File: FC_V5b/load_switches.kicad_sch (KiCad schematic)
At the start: 52 parts, among them U19 AP22652, U21 AP22652, U22 AP22652, U23 AP22652, U24 AP22652, U25 AP22652, U26 AP22652, U27 AP22652, U28 AP22652, U29 AP22652

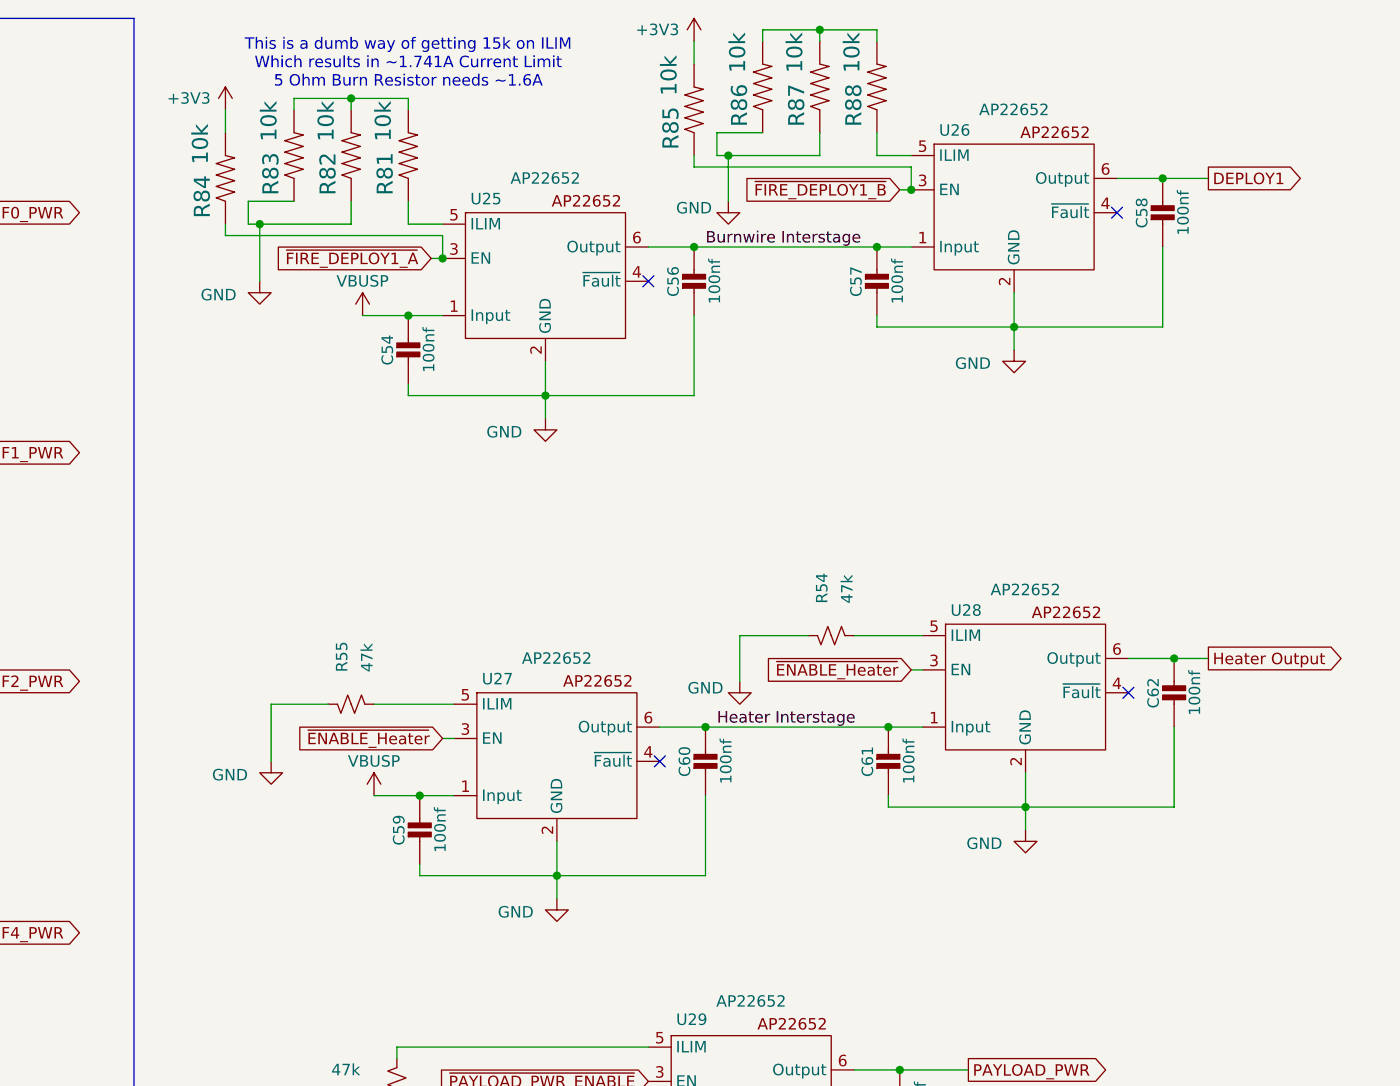
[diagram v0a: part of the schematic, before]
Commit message: Deleted Bad Heater and Burn Load Switches
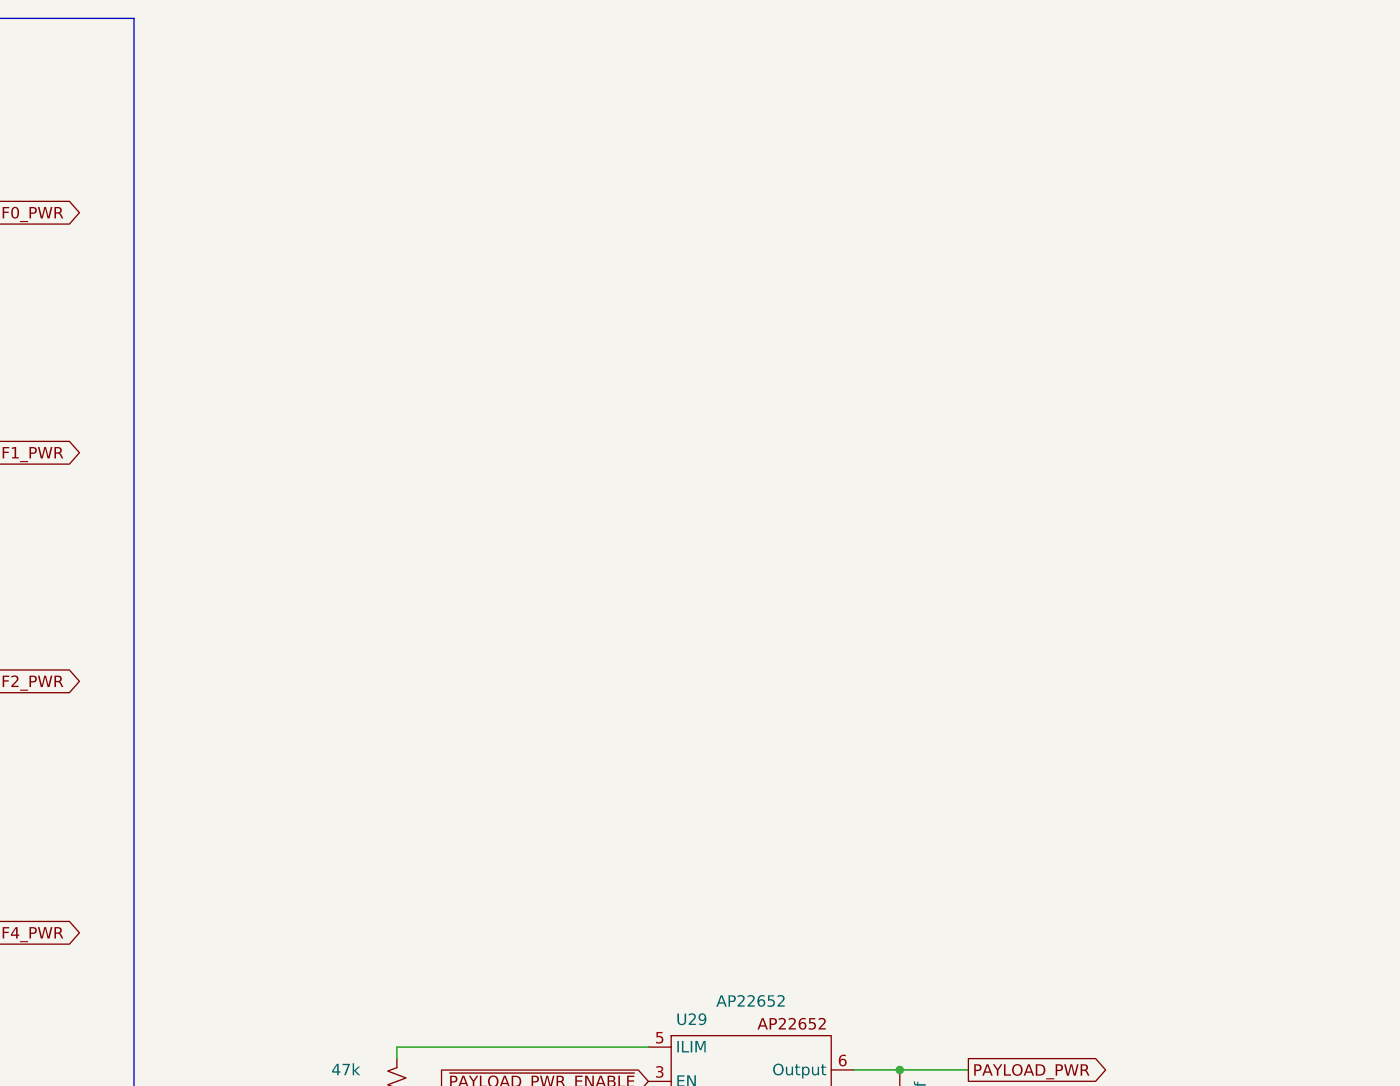
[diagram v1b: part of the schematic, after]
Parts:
- removed C54, C56, C57, C58, C59, C60, C61, C62: 100nf, Capacitor_SMD:C_0402_1005Metric, symbol Adafruit ItsyBitsy RP2040-eagle-import:CAP_CERAMIC_0402NO
- removed R54, R55: 47k, Resistor_SMD:R_0603_1608Metric, symbol Device:R_Small_US
- removed R81, R82, R83, R84, R85, R86, R87, R88: 10k, Resistor_SMD:R_0603_1608Metric, symbol mainboard:RESISTOR0603
- removed U25, U26, U27, U28: AP22652, SOT26:SOT26, symbol Power_Management:AP22652
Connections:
- no-connect marks 10 -> 6
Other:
- note removed: "This is a dumb way of getting 15k on ILIM Which results in ~1.741A Current Limit 5 Ohm Burn Resistor needs ~1.6A"

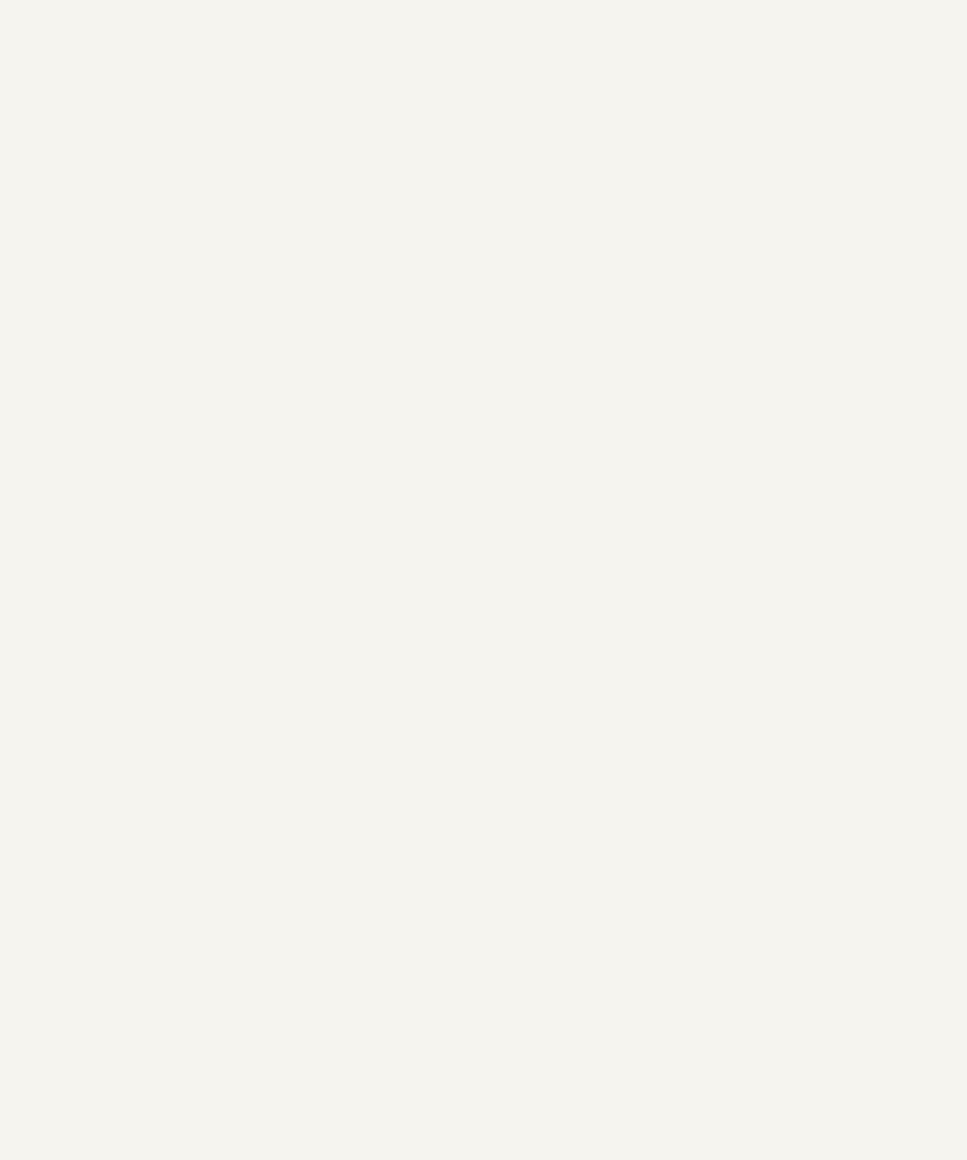
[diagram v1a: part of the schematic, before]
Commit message: Added New Load Switch Symbols
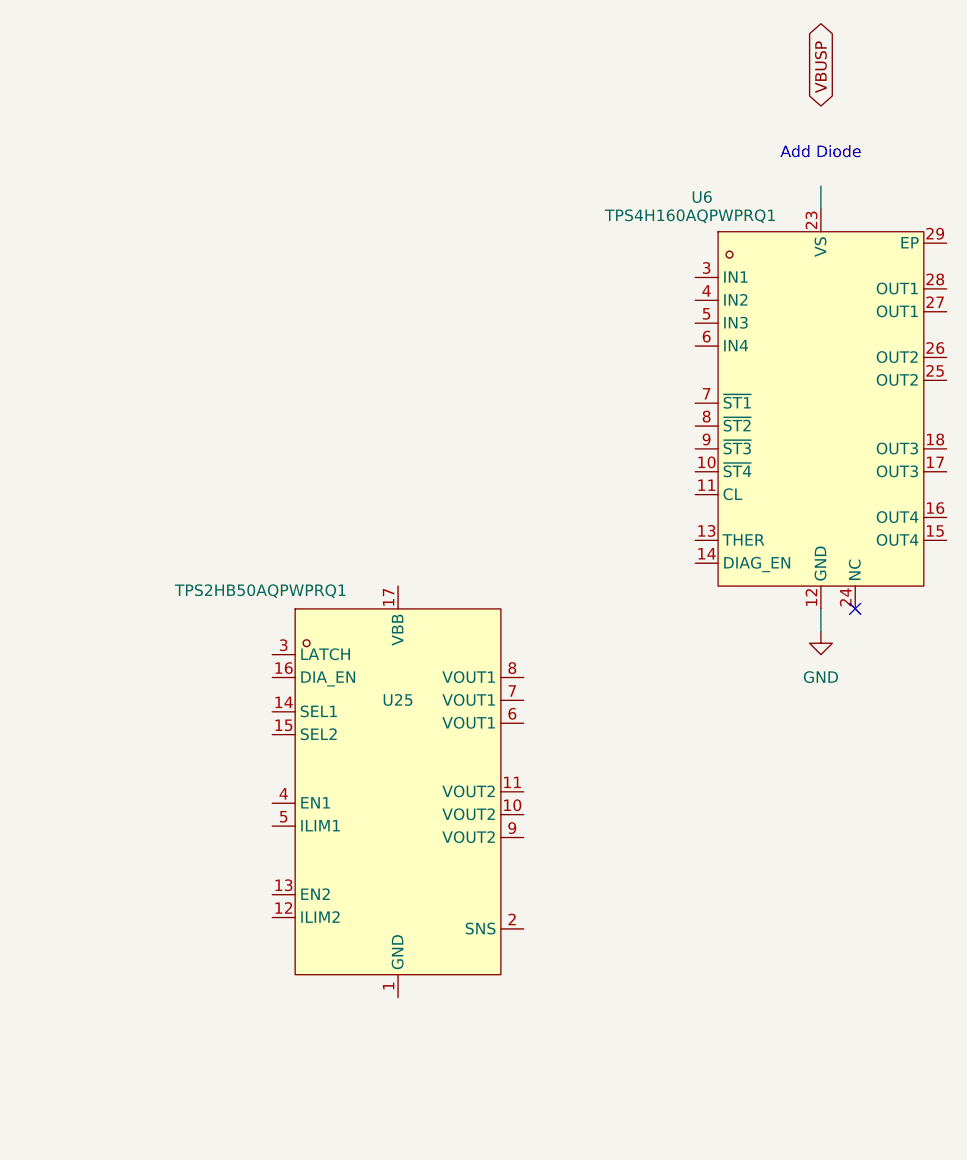
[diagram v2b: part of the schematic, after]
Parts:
- added U25: TPS2HB50AQPWPRQ1, easyeda2kicad:HTSSOP-16_L5.0-W4.4-P0.65-LS6.4-BL-EP-2, symbol easyeda2kicad:TPS2HB50AQPWPRQ1
- added U6: TPS4H160AQPWPRQ1, easyeda2kicad:HTSSOP-28_L9.7-W4.4-P0.65-LS6.4-BL-EP, symbol easyeda2kicad:TPS4H160AQPWPRQ1
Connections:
- net GND: now also U6.1 (GND), U6.12 (GND)
- new net: U6.19 (NC), U6.2 (NC), U6.24 (NC)
- new net: U6.20 (VS), U6.21 (VS), U6.22 (VS), U6.23 (VS)
- no-connect marks 6 -> 7
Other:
- note added: "Add Diode"

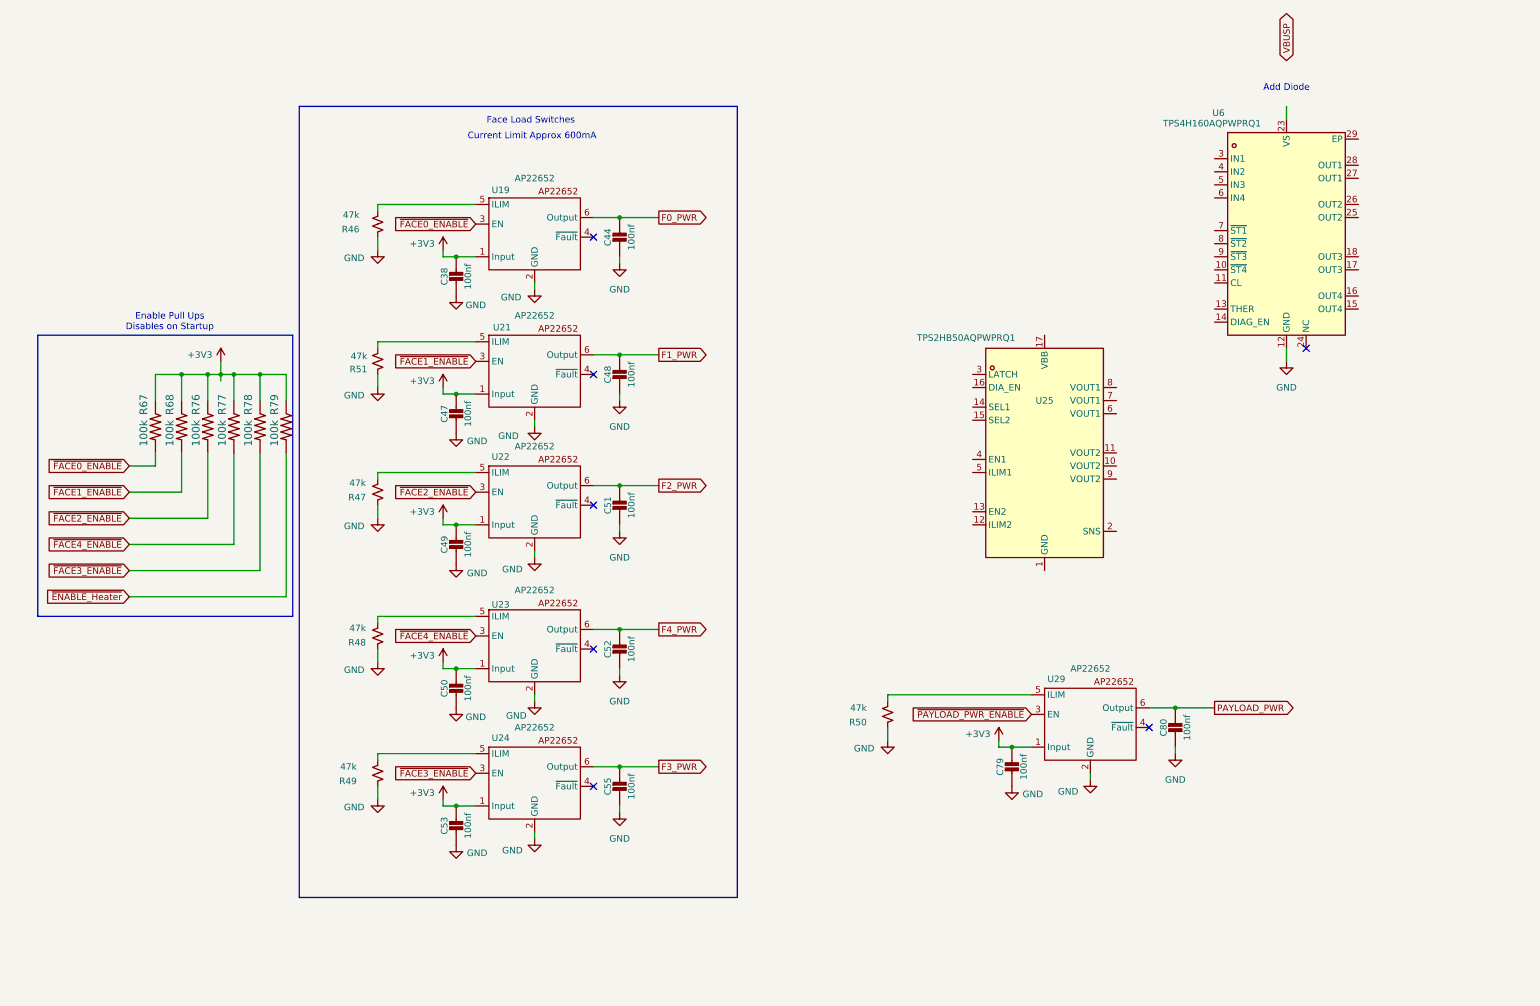
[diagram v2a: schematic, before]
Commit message: Removed Z- GPIO
Also making Progress on Load Switch Update
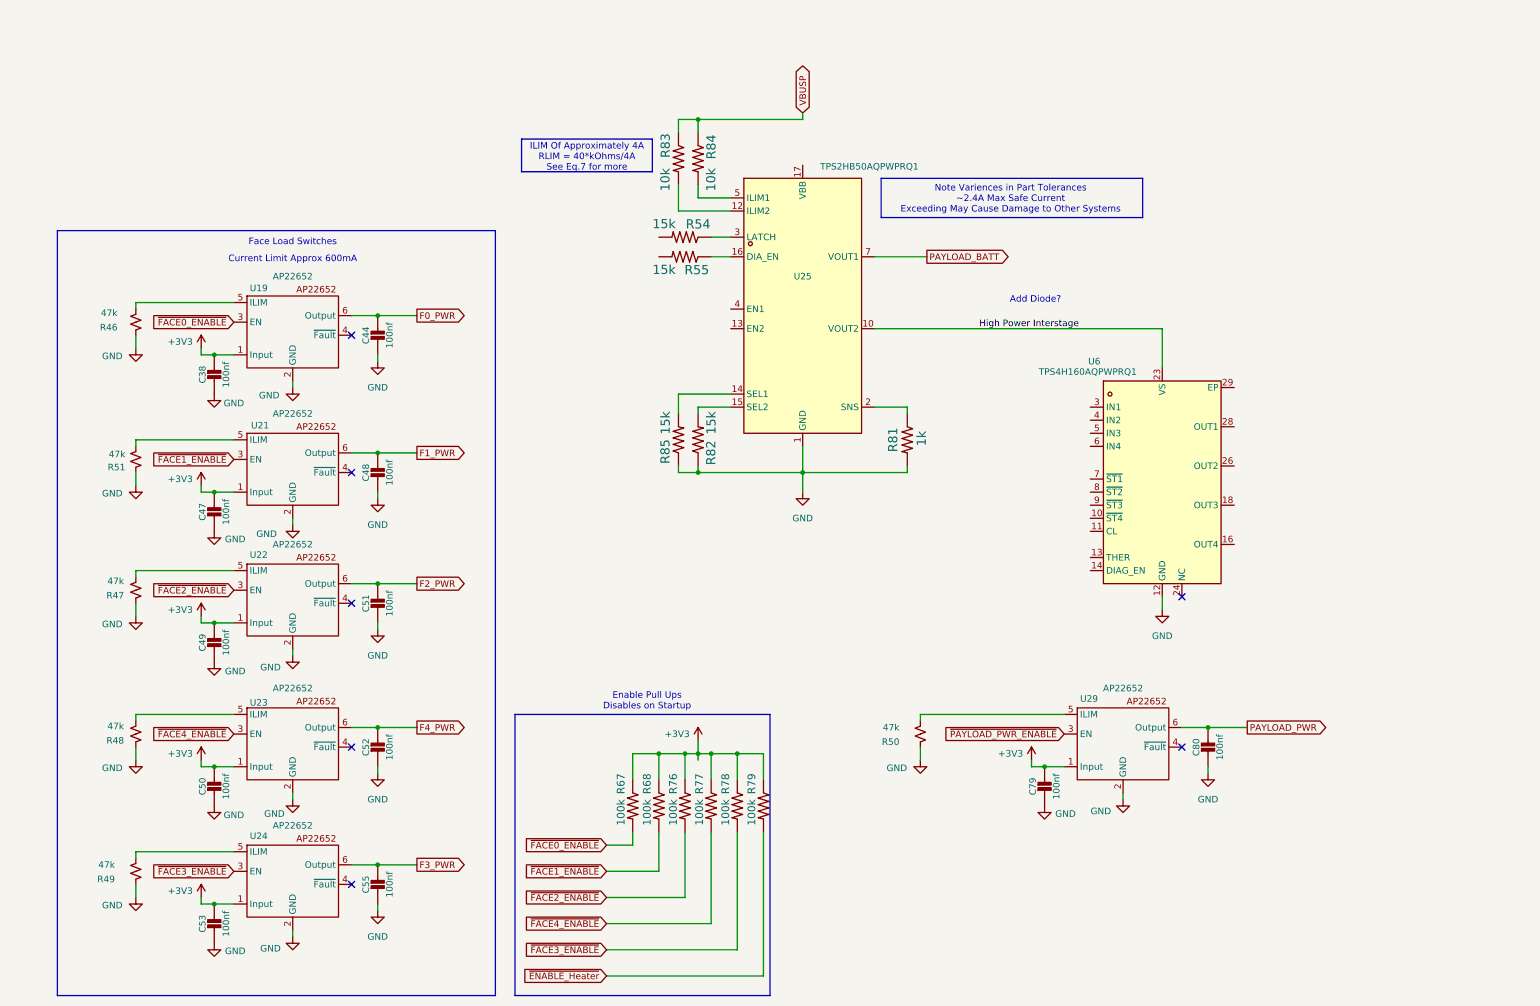
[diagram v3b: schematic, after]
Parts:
- added R54, R55, R82, R85: 15k, Resistor_SMD:R_0603_1608Metric, symbol mainboard:RESISTOR0603
- added R81: 1k, Resistor_SMD:R_0603_1608Metric, symbol mainboard:RESISTOR0603
- added R83, R84: 10k, Resistor_SMD:R_0603_1608Metric, symbol mainboard:RESISTOR0603
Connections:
- net GND: now also U25.1 (GND), R81.2, R82.1, R85.1
- net VBUSP: now also R83.1, R84.1
- net High Power Interstage: now reaches U25.10 (VOUT2)
- net High Power Interstage: now also U25.11 (VOUT2), U25.9 (VOUT2), U6.20 (VS), U6.21 (VS), U6.22 (VS), U6.23 (VS)
- net at U25.12 (ILIM2): now also R83.2
- net at U25.14 (SEL1): now also R85.2
- net at U25.15 (SEL2): now also R82.2
- net at U25.16 (DIA_EN): now also R55.1
- net at U25.2 (SNS): now also R81.1
- net at U25.3 (LATCH): now also R54.1
- net at U25.5 (ILIM1): now also R84.2
- net PAYLOAD_BATT: now reaches U25.6 (VOUT1)
- net PAYLOAD_BATT: now also U25.7 (VOUT1), U25.8 (VOUT1)
- net at U6.15 (OUT4): now also U6.16 (OUT4)
- net at U6.17 (OUT3): now also U6.18 (OUT3)
- net at U6.25 (OUT2): now also U6.26 (OUT2)
- net at U6.27 (OUT1): now also U6.28 (OUT1)
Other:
- note added: "Add Diode?"
- note added: "ILIM Of Approximately 4A RLIM = 40*kOhms/4A See Eq.7 for more"
- note added: "Note Variences in Part Tolerances ~2.4A Max Safe Current Exceeding May Cause Damage to Other Systems"
- note removed: "Add Diode"
- moved on the sheet: C38, C44, C47, C48, C49, C50, C51, C52, C53, C55, C79, C80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
